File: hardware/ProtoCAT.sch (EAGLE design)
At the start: 53 parts, among them U1 ARDUINO, U3 TB6621FNG

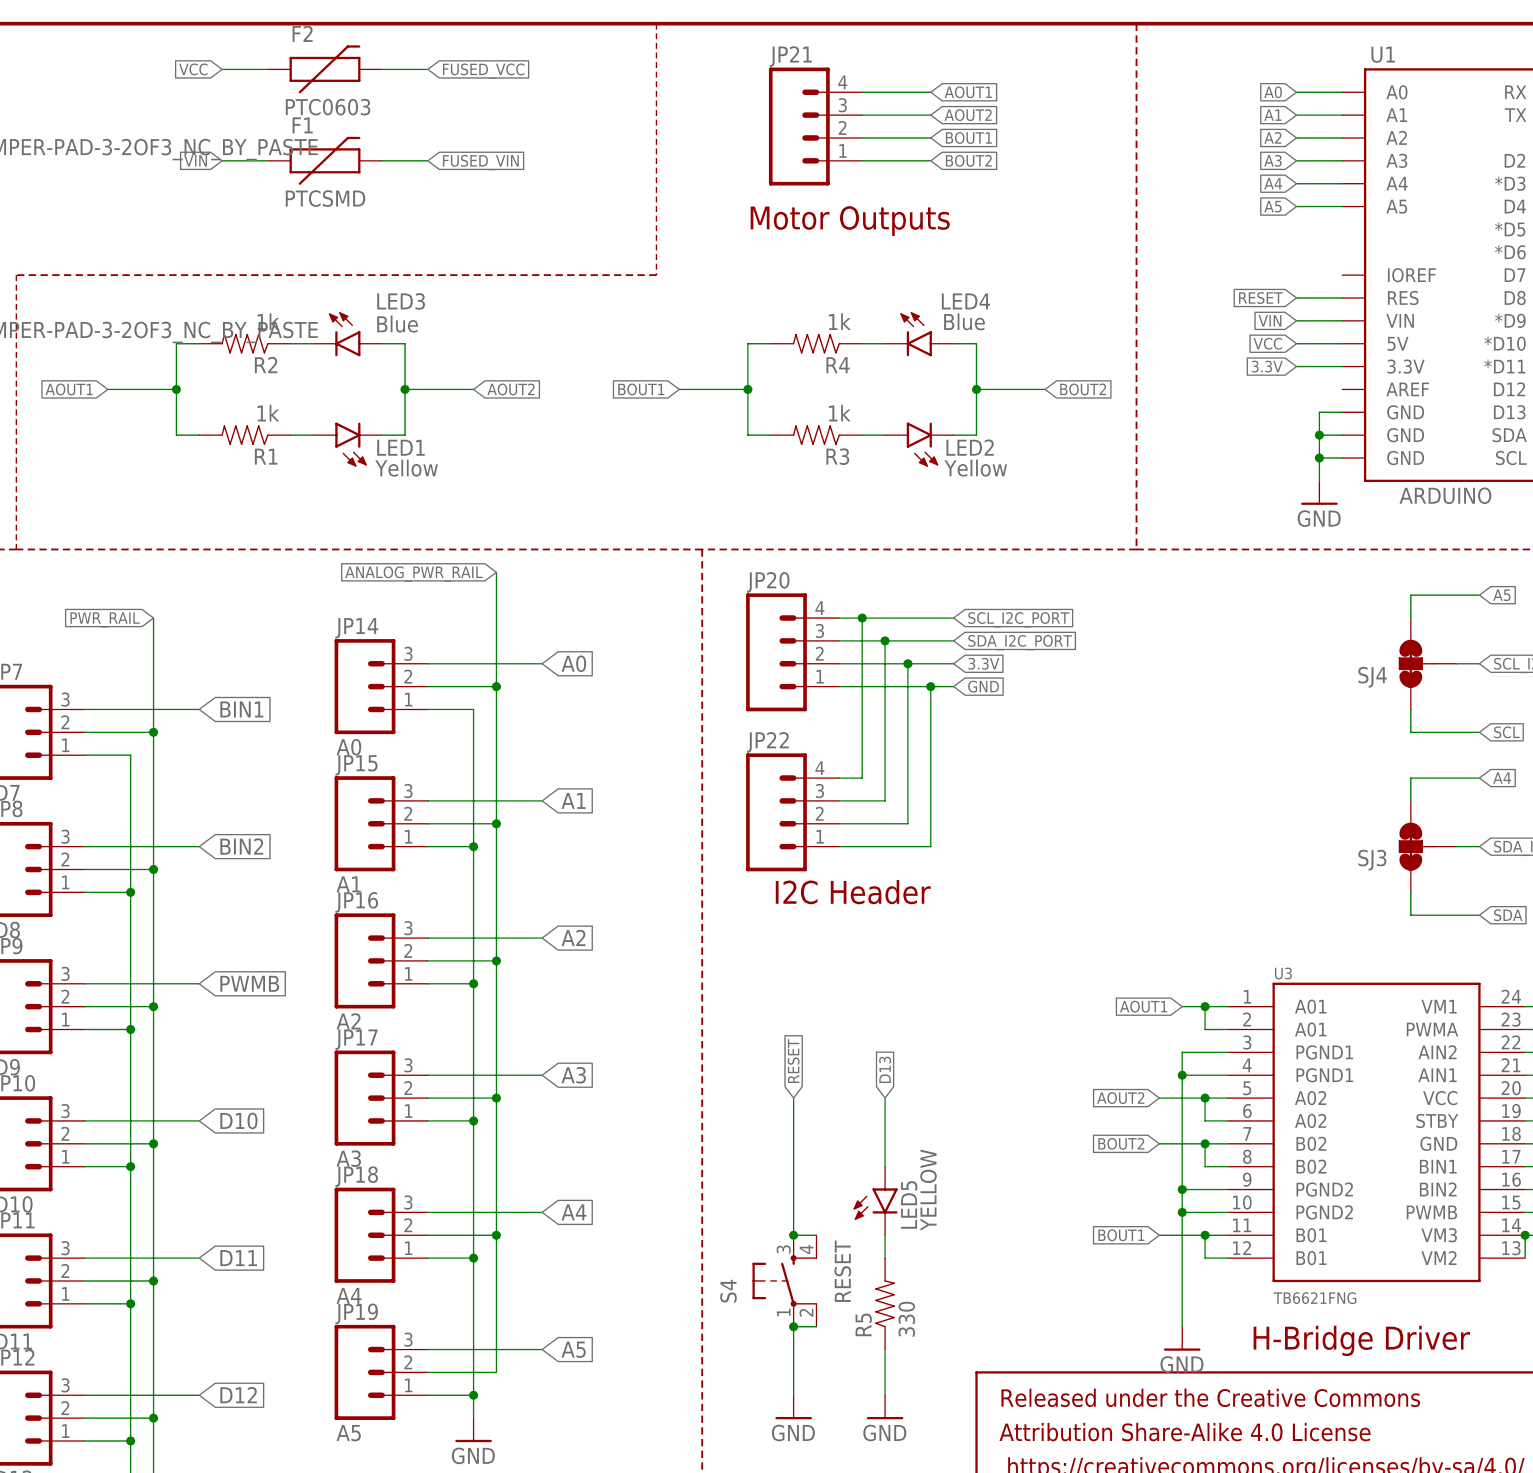
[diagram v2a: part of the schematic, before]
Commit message: Updated fuse to 1206 part on Vcc Line
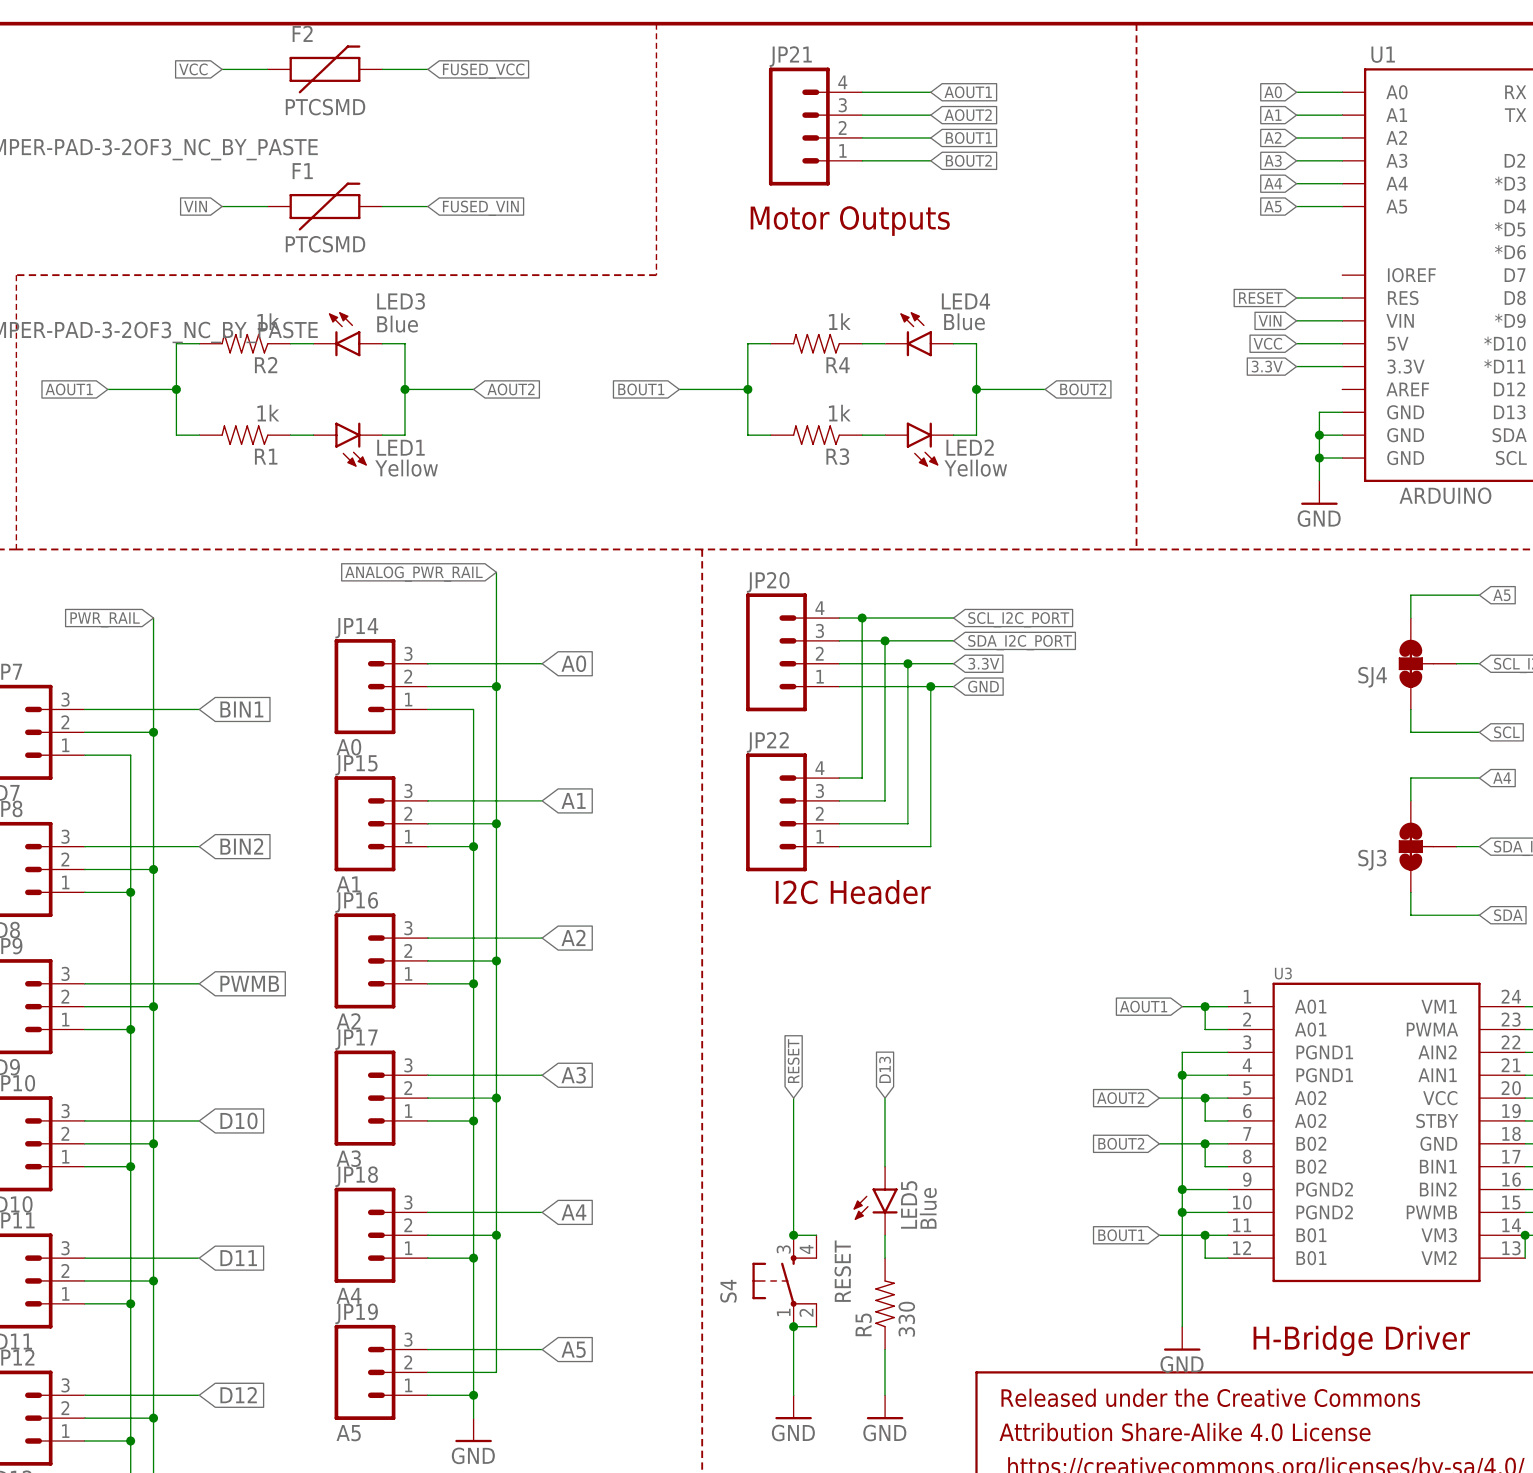
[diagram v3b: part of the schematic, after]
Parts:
- F2: value PTC0603 -> PTCSMD; device SparkFun-PowerIC:PTC0603 -> SparkFun-PowerIC:PTCSMD
- LED5: value YELLOW -> Blue
- U3: value TB6621FNG -> (none); device SparkFun:TB6621FNG -> SparkFun-PowerIC:TB6621FNG
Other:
- moved on the sheet: F1
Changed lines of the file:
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@@
 <part name="GND14" library="SparkFun" deviceset="GND" device=""/>
 <part name="JP5" library="SparkFun-Connectors" deviceset="M03" device="PTH" value="D5"/>
-<part name="U3" library="SparkFun" deviceset="TB6621FNG" device=""/>
+<part name="U3" library="SparkFun-PowerIC" deviceset="TB6621FNG" device=""/>
 <part name="C1" library="SparkFun-Capacitors" deviceset="0.1UF-25V-5%(0603)" device="" value="0.1uF"/>
 <part name="C2" library="SparkFun-Capacitors" deviceset="0.1UF-25V-5%(0603)" device="" value="0.1uF"/>
@@
 <part name="JP19" library="SparkFun-Connectors" deviceset="M03" device="PTH" value="A5"/>
 <part name="GND2" library="SparkFun" deviceset="GND" device=""/>
-<part name="LED5" library="SparkFun-LED" deviceset="LED" device="0603" value="YELLOW"/>
+<part name="LED5" library="SparkFun-LED" deviceset="LED" device="0603" value="Blue"/>
 <part name="R5" library="SparkFun-Resistors" deviceset="330OHM1/10W1%(0603)" device="" value="330"/>
 <part name="GND6" library="SparkFun" deviceset="GND" device=""/>
@@
 <part name="GND7" library="SparkFun" deviceset="GND" device=""/>
 <part name="F1" library="SparkFun-PowerIC" deviceset="PTC" device="SMD" value="PTCSMD"/>
-<part name="F2" library="SparkFun-PowerIC" deviceset="PTC" device="0603"/>
+<part name="F2" library="SparkFun-PowerIC" deviceset="PTC" device="SMD" value="PTCSMD"/>
 <part name="FID1" library="SparkFun-Aesthetics" deviceset="FIDUCIAL" device="UFIDUCIAL"/>
 <part name="FID2" library="SparkFun-Aesthetics" deviceset="FIDUCIAL" device="UFIDUCIAL"/>
@@
 <instance part="S4" gate="S" x="127" y="45.72" rot="R90"/>
 <instance part="GND7" gate="1" x="127" y="30.48"/>
-<instance part="F1" gate="G$1" x="73.66" y="170.18"/>
+<instance part="F1" gate="G$1" x="73.66" y="165.1"/>
 <instance part="F2" gate="G$1" x="73.66" y="180.34"/>
 <instance part="FID1" gate="G$1" x="243.84" y="27.94"/>
@@
 </segment>
 <segment>
-<wire x1="63.5" y1="170.18" x2="68.58" y2="170.18" width="0.1524" layer="91"/>
+<wire x1="63.5" y1="165.1" x2="68.58" y2="165.1" width="0.1524" layer="91"/>
 <pinref part="F1" gate="G$1" pin="1"/>
-<label x="63.5" y="170.18" size="1.27" layer="95" rot="R180" xref="yes"/>
+<label x="63.5" y="165.1" size="1.27" layer="95" rot="R180" xref="yes"/>
 </segment>
 </net>
@@
 <net name="FUSED_VIN" class="0">
 <segment>
-<wire x1="81.28" y1="170.18" x2="86.36" y2="170.18" width="0.1524" layer="91"/>
+<wire x1="81.28" y1="165.1" x2="86.36" y2="165.1" width="0.1524" layer="91"/>
 <pinref part="F1" gate="G$1" pin="2"/>
-<label x="86.36" y="170.18" size="1.27" layer="95" xref="yes"/>
-</segment>
-<segment>
+<label x="86.36" y="165.1" size="1.27" layer="95" xref="yes"/>
+</segment>
+<segment>

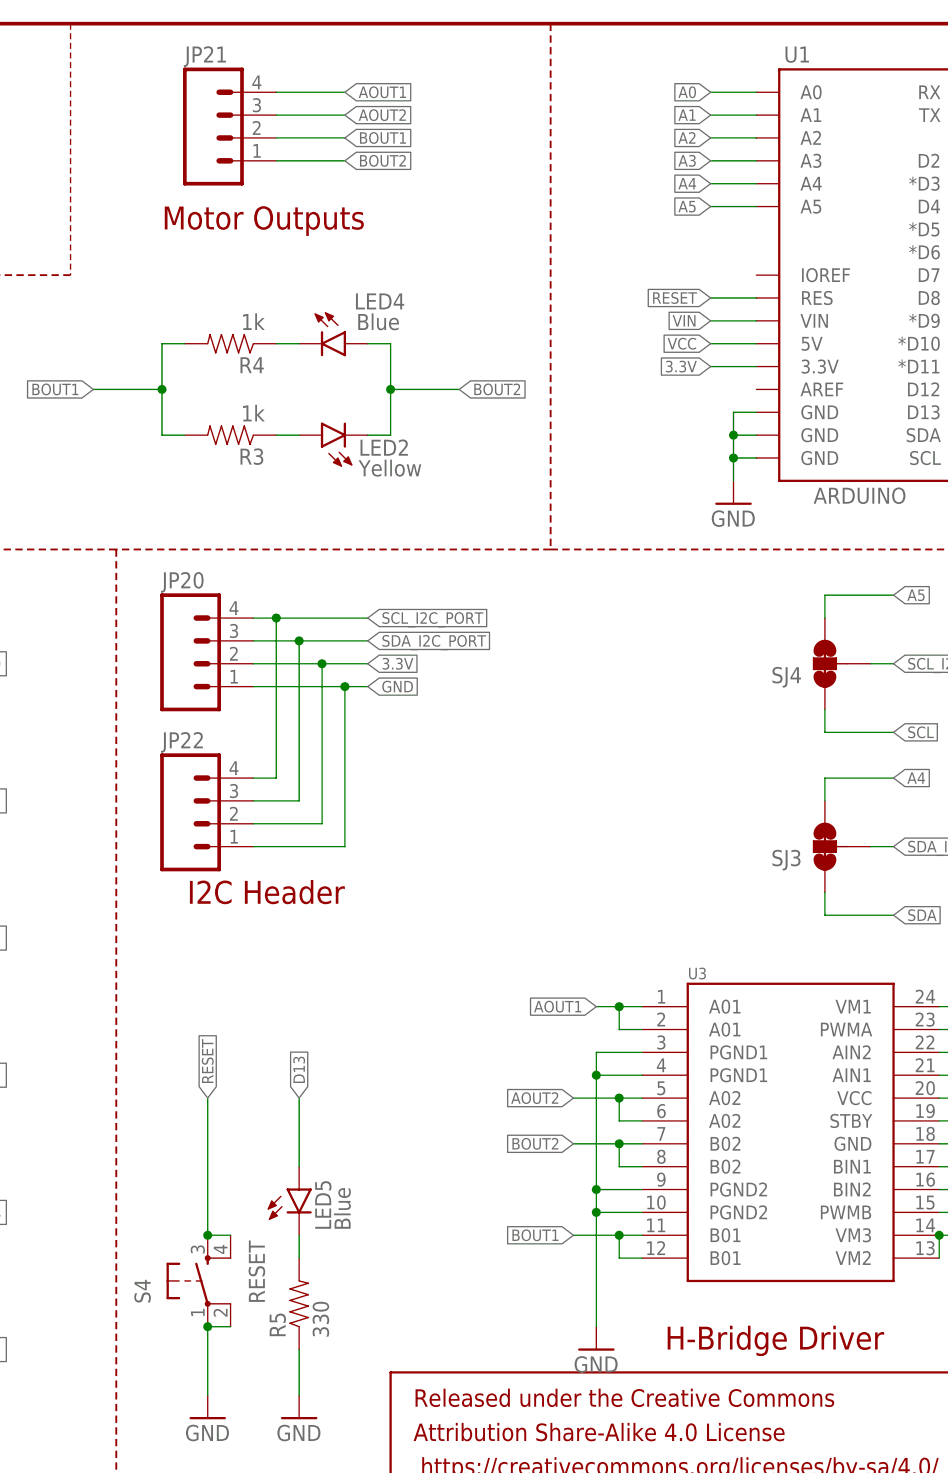
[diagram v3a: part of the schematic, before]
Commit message: Removed unused layers
Removed unused layers and backup b# / s# files
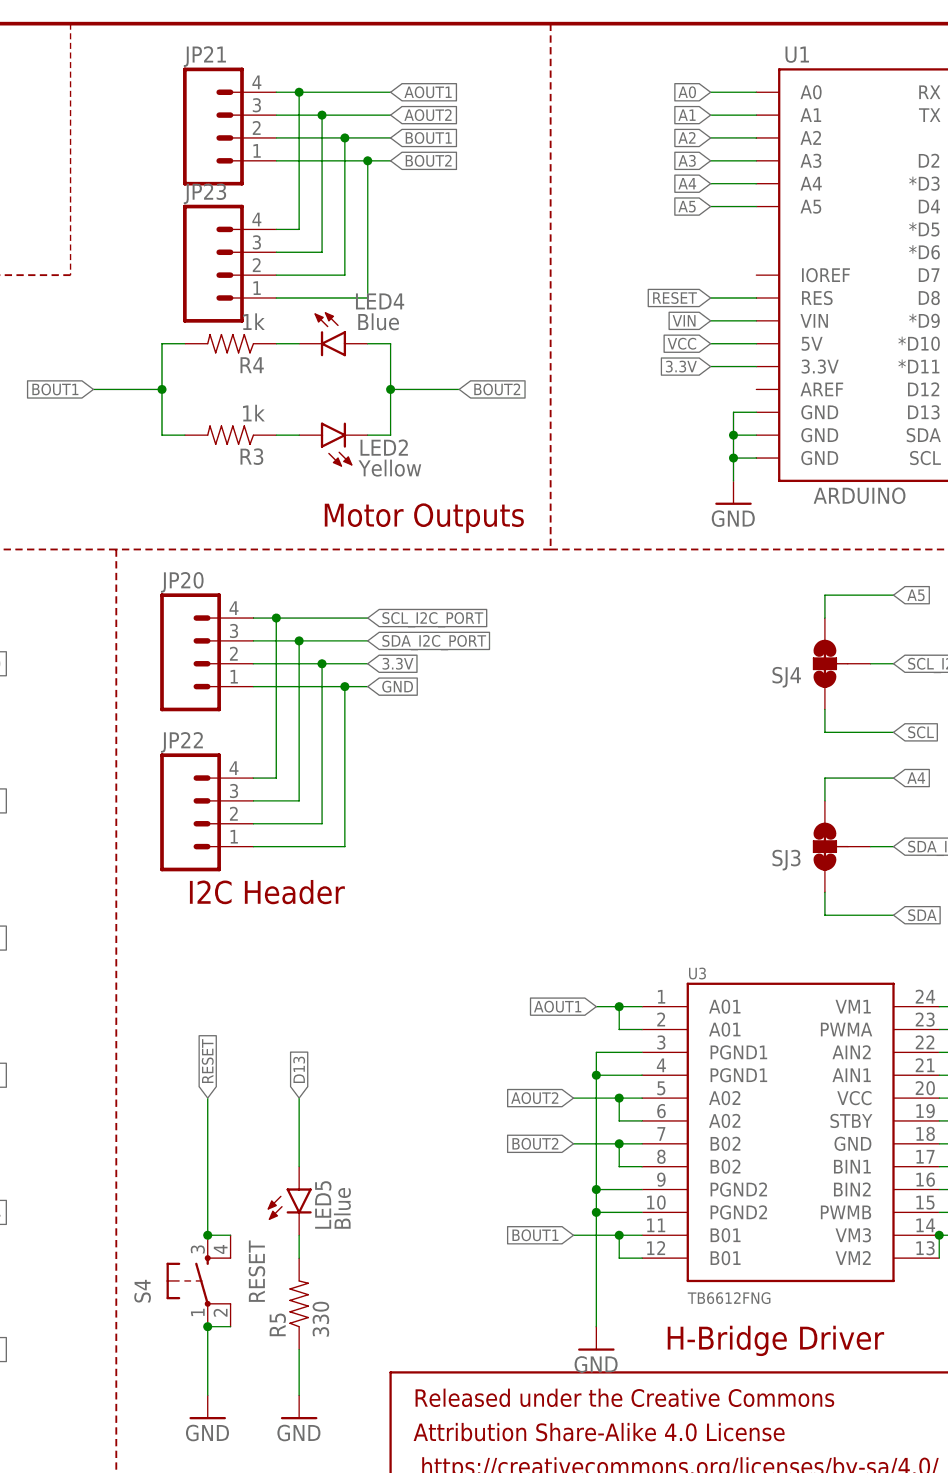
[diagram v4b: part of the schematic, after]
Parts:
- added JP23: (no value), SparkFun-Connectors:M04SMD_STRAIGHT_COMBO
- U3: value (none) -> TB6612FNG; device SparkFun-PowerIC:TB6621FNG -> SparkFun-PowerIC:TB6612FNG
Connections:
- net AOUT1: now also JP23.4
- net AOUT2: now also JP23.3
- net BOUT1: now also JP23.2
- net BOUT2: now also JP23.1
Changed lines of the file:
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@@
 <part name="GND14" library="SparkFun" deviceset="GND" device=""/>
 <part name="JP5" library="SparkFun-Connectors" deviceset="M03" device="PTH" value="D5"/>
-<part name="U3" library="SparkFun-PowerIC" deviceset="TB6621FNG" device=""/>
+<part name="U3" library="SparkFun-PowerIC" deviceset="TB6612FNG" device=""/>
 <part name="C1" library="SparkFun-Capacitors" deviceset="0.1UF-25V-5%(0603)" device="" value="0.1uF"/>
 <part name="C2" library="SparkFun-Capacitors" deviceset="0.1UF-25V-5%(0603)" device="" value="0.1uF"/>
@@
 <part name="LOGO3" library="SparkFun-Aesthetics" deviceset="SFE_LOGO_FLAME" device=".2COP"/>
 <part name="LOGO4" library="SparkFun-Aesthetics" deviceset="SFE_LOGO_NAME_FLAME" device=".1_INCH" value="SFE_LOGO_NAME_FLAME.1_INCH"/>
+<part name="JP23" library="SparkFun-Connectors" deviceset="M04" device="SMD_STRAIGHT_COMBO"/>
 </parts>
 <sheets>
@@
 <text x="177.8" y="38.1" size="2.54" layer="94">H-Bridge Driver</text>
 <text x="124.714" y="87.63" size="2.54" layer="94">I2C Header</text>
-<text x="121.92" y="162.56" size="2.54" layer="94">Motor Outputs</text>
+<text x="139.7" y="129.54" size="2.54" layer="94">Motor Outputs</text>
 <wire x1="165.1" y1="185.42" x2="165.1" y2="127" width="0.2032" layer="94" style="longdash"/>
 <wire x1="165.1" y1="127" x2="248.92" y2="127" width="0.2032" layer="94" style="longdash"/>
@@
 <instance part="LOGO3" gate="G$1" x="264.16" y="27.94"/>
 <instance part="LOGO4" gate="G$1" x="284.48" y="-17.78"/>
+<instance part="JP23" gate="G$1" x="129.54" y="157.48"/>
 </instances>
 <busses>
@@
 <segment>
 <pinref part="JP21" gate="G$1" pin="4"/>
-<wire x1="134.62" y1="177.8" x2="142.24" y2="177.8" width="0.1524" layer="91"/>
-<label x="142.24" y="177.8" size="1.27" layer="95" xref="yes"/>
+<wire x1="134.62" y1="177.8" x2="137.16" y2="177.8" width="0.1524" layer="91"/>
+<label x="147.32" y="177.8" size="1.27" layer="95" xref="yes"/>
+<pinref part="JP23" gate="G$1" pin="4"/>
+<wire x1="137.16" y1="177.8" x2="147.32" y2="177.8" width="0.1524" layer="91"/>
+<wire x1="134.62" y1="162.56" x2="137.16" y2="162.56" width="0.1524" layer="91"/>
+<wire x1="137.16" y1="162.56" x2="137.16" y2="177.8" width="0.1524" layer="91"/>
+<junction x="137.16" y="177.8"/>
 </segment>
 </net>
@@
 <segment>
 <pinref part="JP21" gate="G$1" pin="3"/>
-<wire x1="134.62" y1="175.26" x2="142.24" y2="175.26" width="0.1524" layer="91"/>
-<label x="142.24" y="175.26" size="1.27" layer="95" xref="yes"/>
+<wire x1="134.62" y1="175.26" x2="139.7" y2="175.26" width="0.1524" layer="91"/>
+<label x="147.32" y="175.26" size="1.27" layer="95" xref="yes"/>
+<wire x1="139.7" y1="175.26" x2="147.32" y2="175.26" width="0.1524" layer="91"/>
+<wire x1="139.7" y1="175.26" x2="139.7" y2="160.02" width="0.1524" layer="91"/>
+<junction x="139.7" y="175.26"/>
+<pinref part="JP23" gate="G$1" pin="3"/>
+<wire x1="139.7" y1="160.02" x2="134.62" y2="160.02" width="0.1524" layer="91"/>
 </segment>
 </net>
@@
 <segment>
 <pinref part="JP21" gate="G$1" pin="1"/>
-<wire x1="134.62" y1="170.18" x2="142.24" y2="170.18" width="0.1524" layer="91"/>
-<label x="142.24" y="170.18" size="1.27" layer="95" xref="yes"/>
+<wire x1="134.62" y1="170.18" x2="144.78" y2="170.18" width="0.1524" layer="91"/>
+<label x="147.32" y="170.18" size="1.27" layer="95" xref="yes"/>
+<wire x1="144.78" y1="170.18" x2="147.32" y2="170.18" width="0.1524" layer="91"/>
+<wire x1="144.78" y1="170.18" x2="144.78" y2="154.94" width="0.1524" layer="91"/>
+<junction x="144.78" y="170.18"/>
+<pinref part="JP23" gate="G$1" pin="1"/>
+<wire x1="144.78" y1="154.94" x2="134.62" y2="154.94" width="0.1524" layer="91"/>
 </segment>
 </net>
@@
 <pinref part="JP21" gate="G$1" pin="2"/>
 <wire x1="134.62" y1="172.72" x2="142.24" y2="172.72" width="0.1524" layer="91"/>
-<label x="142.24" y="172.72" size="1.27" layer="95" xref="yes"/>
-</segment>
-</net>
+<label x="147.32" y="172.72" size="1.27" layer="95" xref="yes"/>
+<pinref part="JP23" gate="G$1" pin="2"/>
+<wire x1="142.24" y1="172.72" x2="147.32" y2="172.72" width="0.1524" layer="91"/>
+<wire x1="142.24" y1="157.48" x2="134.62" y2="157.48" width="0.1524" layer="91"/>
+<wire x1="142.24" y1="157.48" x2="142.24" y2="172.72" width="0.1524" layer="91"/>
+<junction x="142.24" y="172.72"/>
+</segment>
+</net>
